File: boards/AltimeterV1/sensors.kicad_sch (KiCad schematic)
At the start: 23 parts

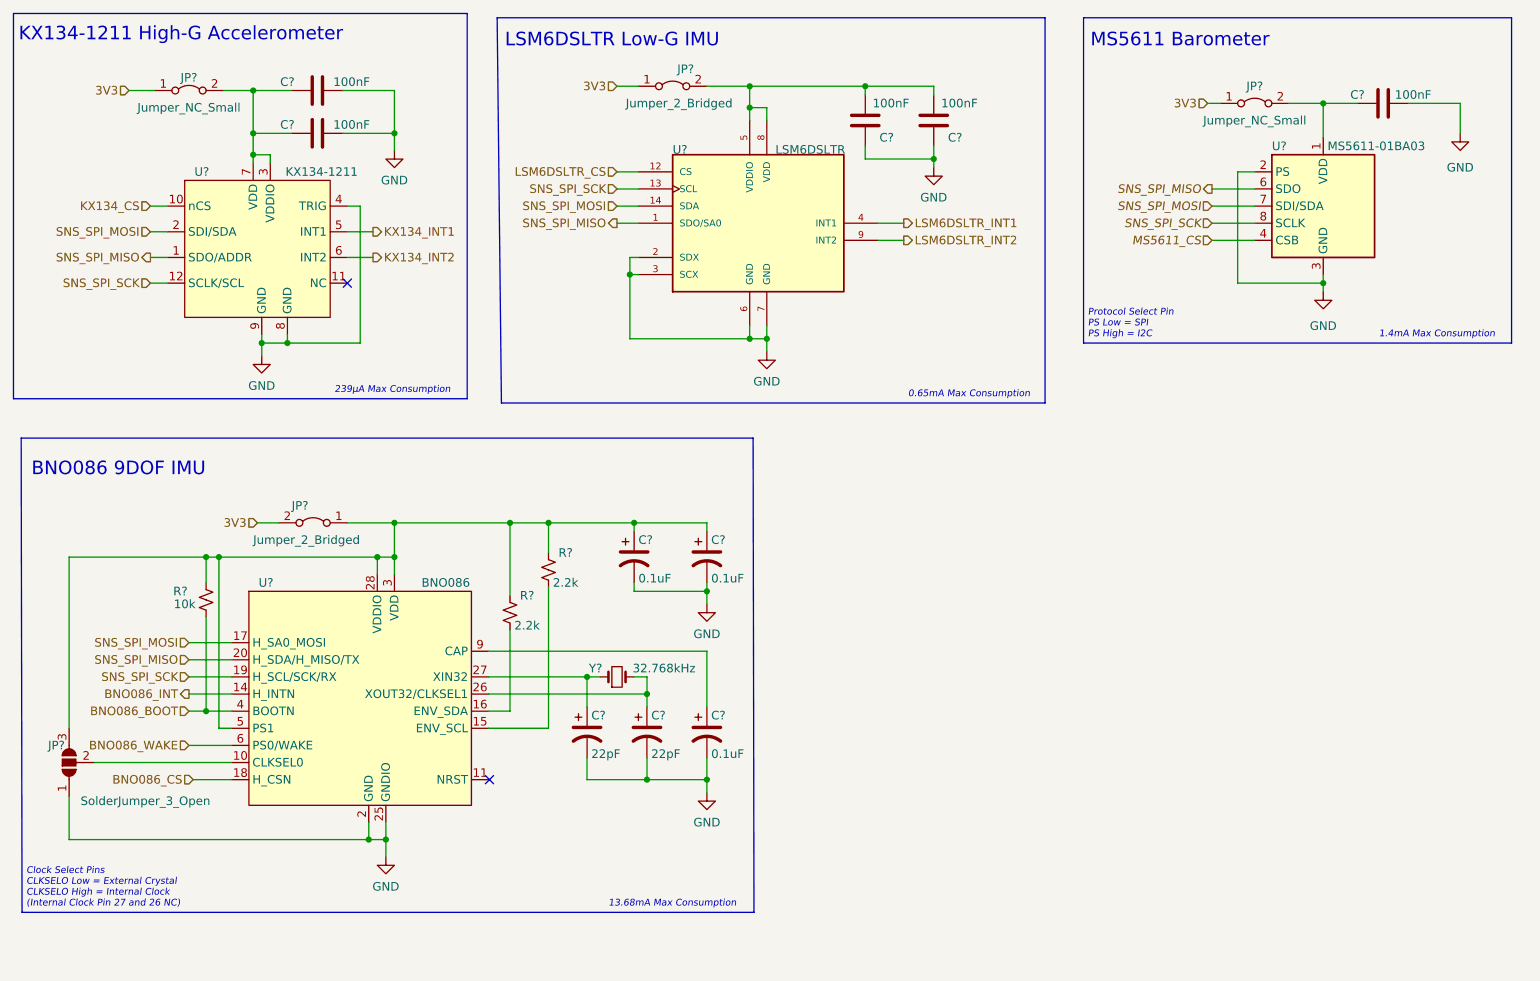
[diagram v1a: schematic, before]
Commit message: updated sensor schematics for I2C communication, added SNS I2C labels for MCU and headers
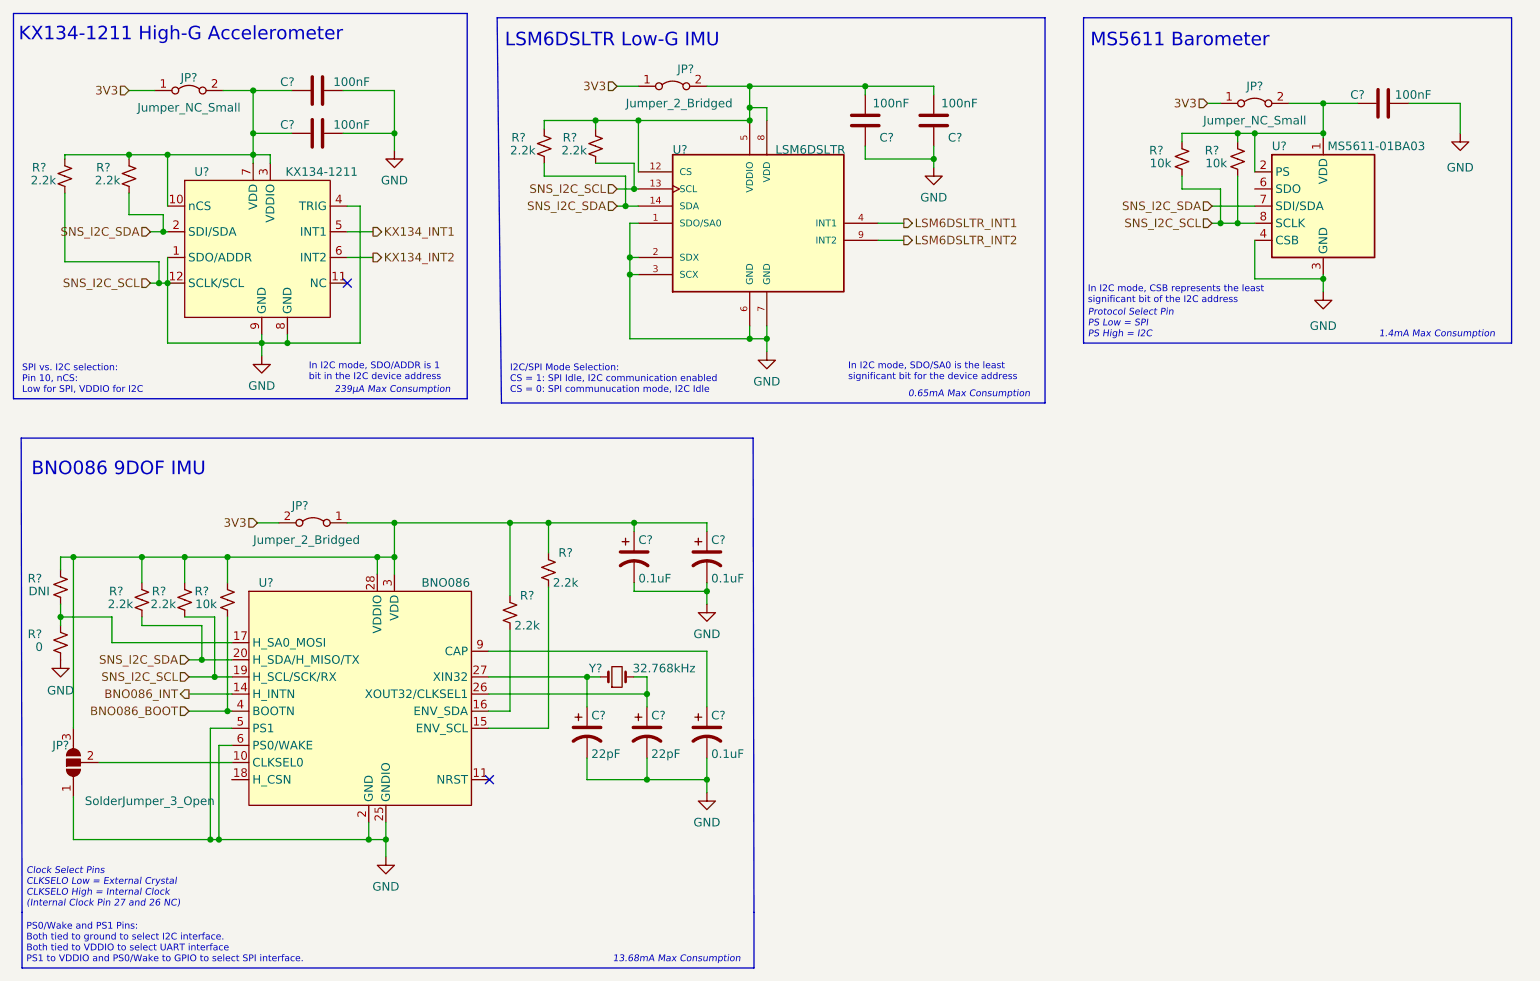
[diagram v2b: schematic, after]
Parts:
- added R? (x6): 2.2k, Resistor_SMD:R_0805_2012Metric_Pad1.20x1.40mm_HandSolder, symbol Device:R_Small_US
- added R?: DNI, Resistor_SMD:R_0805_2012Metric_Pad1.20x1.40mm_HandSolder, symbol Device:R_Small_US
- added R?: 0, Resistor_SMD:R_0805_2012Metric_Pad1.20x1.40mm_HandSolder, symbol Device:R_Small_US
- added R? (x2): 10k, Resistor_SMD:R_0805_2012Metric_Pad1.20x1.40mm_HandSolder, symbol Device:R_Small_US
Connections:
- net BNO086_WAKE is gone; now on net GND: U?.6 (PS0/WAKE)
- net KX134_CS is gone; now on an unnamed net: U?.10 (nCS)
- net LSM6DSLTR_CS is gone; now on an unnamed net: U?.12 (CS)
- net MS5611_CS is gone; now on net GND: U?.4 (CSB), U?.5 (CSB)
- net SNS_SPI_SCK is gone; now on net GND: U?.12 (SCLK/SCL), U?.13 (SCL), U?.19 (H_SCL/SCK/RX), U?.8 (SCLK)
- net GND: now also U?.1 (SDO/ADDR), U?.1 (SDO/SA0), U?.5 (PS1), R?.1, R?.1, R?.1, R?.1, R?.1, R?.1; no longer U?.2 (PS)
- net at C?.1, C?.2, JP?.2 (B)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: now also R?.2, R?.2
- net at C?.2, C?.2, JP?.2 (B)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: now also R?.2, R?.2
- net at C?.2, JP?.2 (B), U?.1 (VDD): now also U?.2 (PS), R?.2, R?.2
- net at C?.1, C?.1, JP?.1 (A)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: now also R?.2, R?.2, R?.2; no longer U?.5 (PS1)
- net BNO086_CS: no longer names the net of U?.18 (H_CSN)
- removed net SNS_SPI_MISO: U?.1 (SDO/ADDR), U?.1 (SDO/SA0), U?.20 (H_SDA/H_MISO/TX), U?.6 (SDO)
- net SNS_SPI_MOSI renamed SNS_I2C_SDA
- net SNS_I2C_SDA: now also U?.20 (H_SDA/H_MISO/TX), R?.1, R?.1, R?.1; no longer U?.17 (H_SA0_MOSI)
- new net: R?.1, R?.2, U?.17 (H_SA0_MOSI)
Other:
- note added: "I2C/SPI Mode Selection: CS = 1: SPI Idle, I2C communication enabled CS = 0: SPI communucation mode, I2C Idle"
- note added: "In I2C mode, CSB represents the least significant bit of the I2C address"
- note added: "In I2C mode, SDO/ADDR is 1 bit in the I2C device address"
- note added: "In I2C mode, SDO/SA0 is the least significant bit for the device address"
- note added: "PS0/Wake and PS1 Pins: Both tied to ground to select I2C interface. Both tied to VDDIO to select UART interface PS1 to VDDIO and PS0/Wake to GPIO to select SPI interface."
- note added: "SPI vs. I2C selection: Pin 10, nCS: Low for SPI, VDDIO for I2C"
- moved on the sheet: JP?, R?

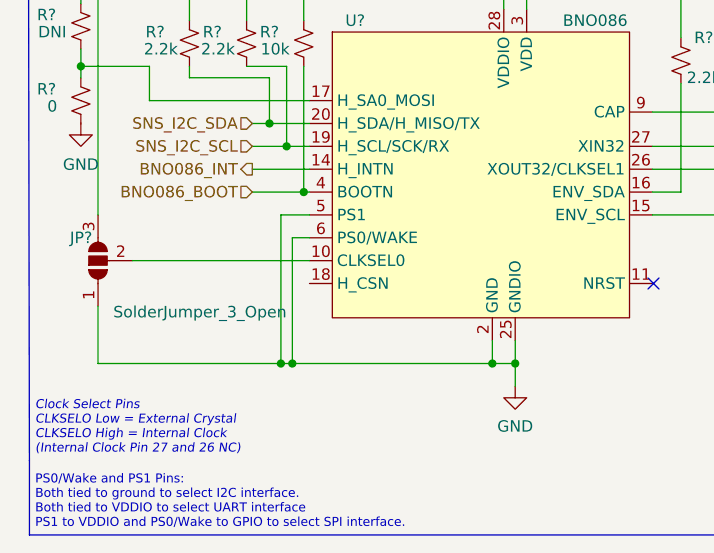
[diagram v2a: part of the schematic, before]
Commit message: updated hierarchical sheets and moved power schematics
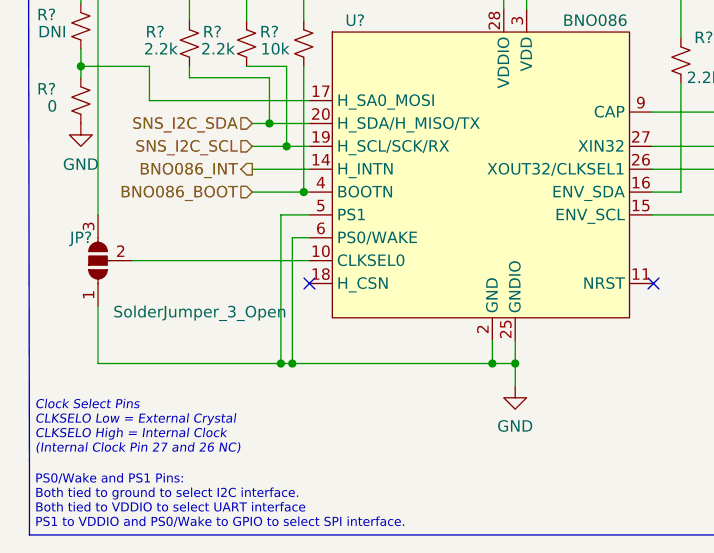
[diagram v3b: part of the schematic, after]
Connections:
- no-connect marks 2 -> 3
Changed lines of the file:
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@@
   (junction (at 107.95 54.61) (diameter 0) (color 0 0 0 0)
   )
+  (no_connect (at 48.895 129.54))
   (no_connect (at 87.122 129.54))
   (no_connect (at 66.04 55.88))

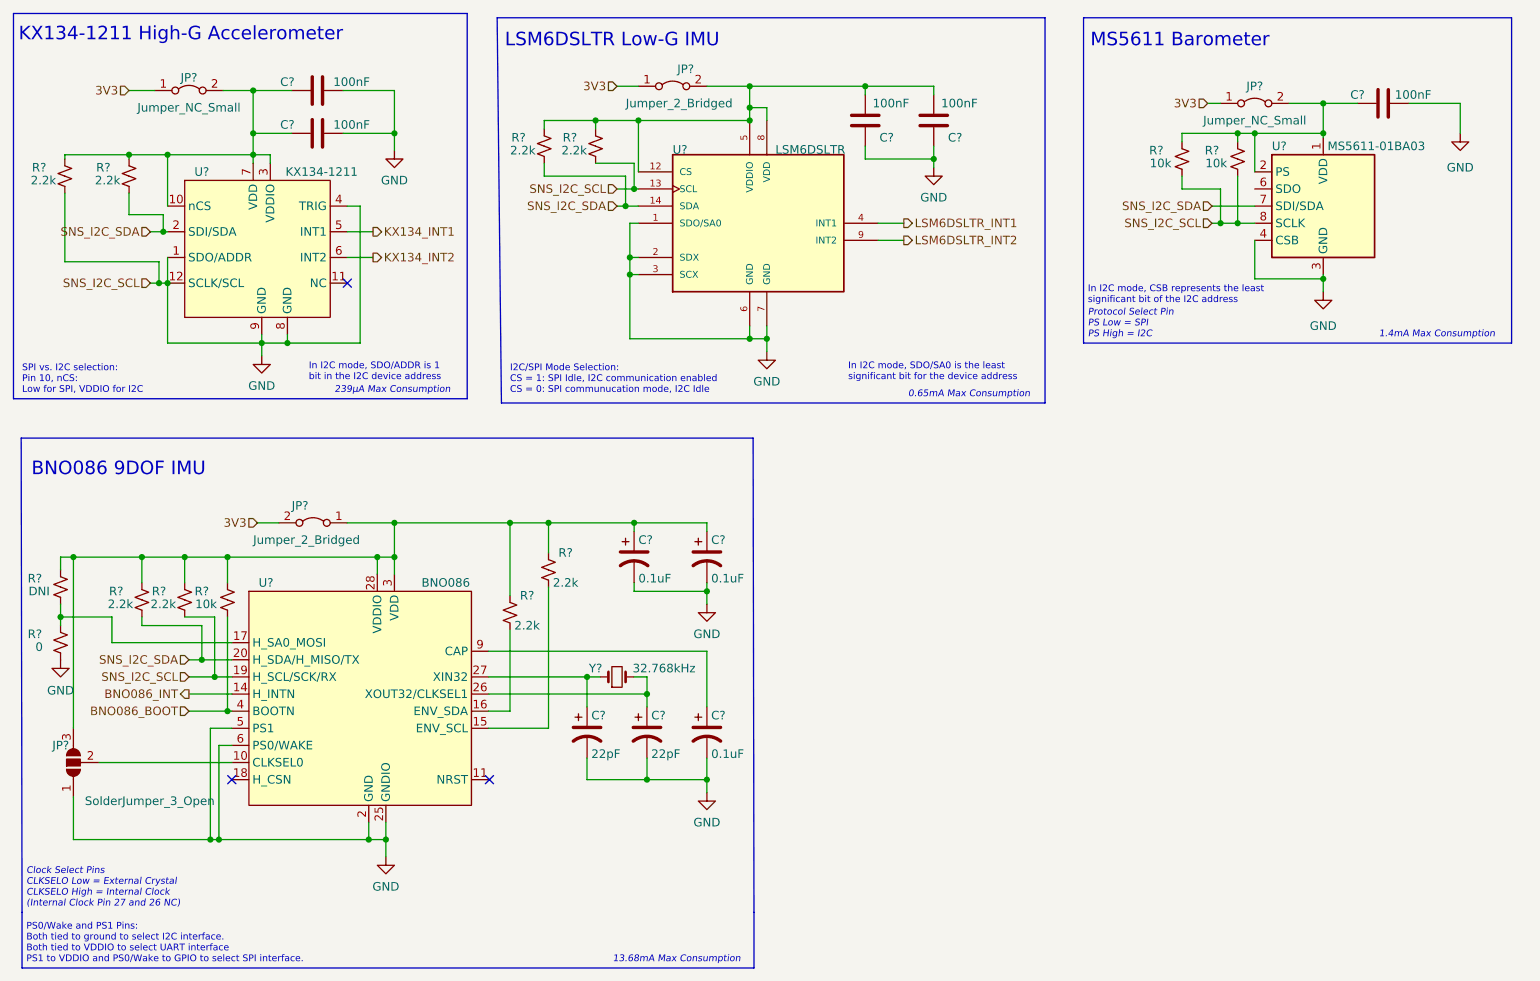
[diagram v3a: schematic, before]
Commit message: added flash memory, added buzzer, corrected all schematic labels, assigned footprints, added switch, updated pcb from schematic
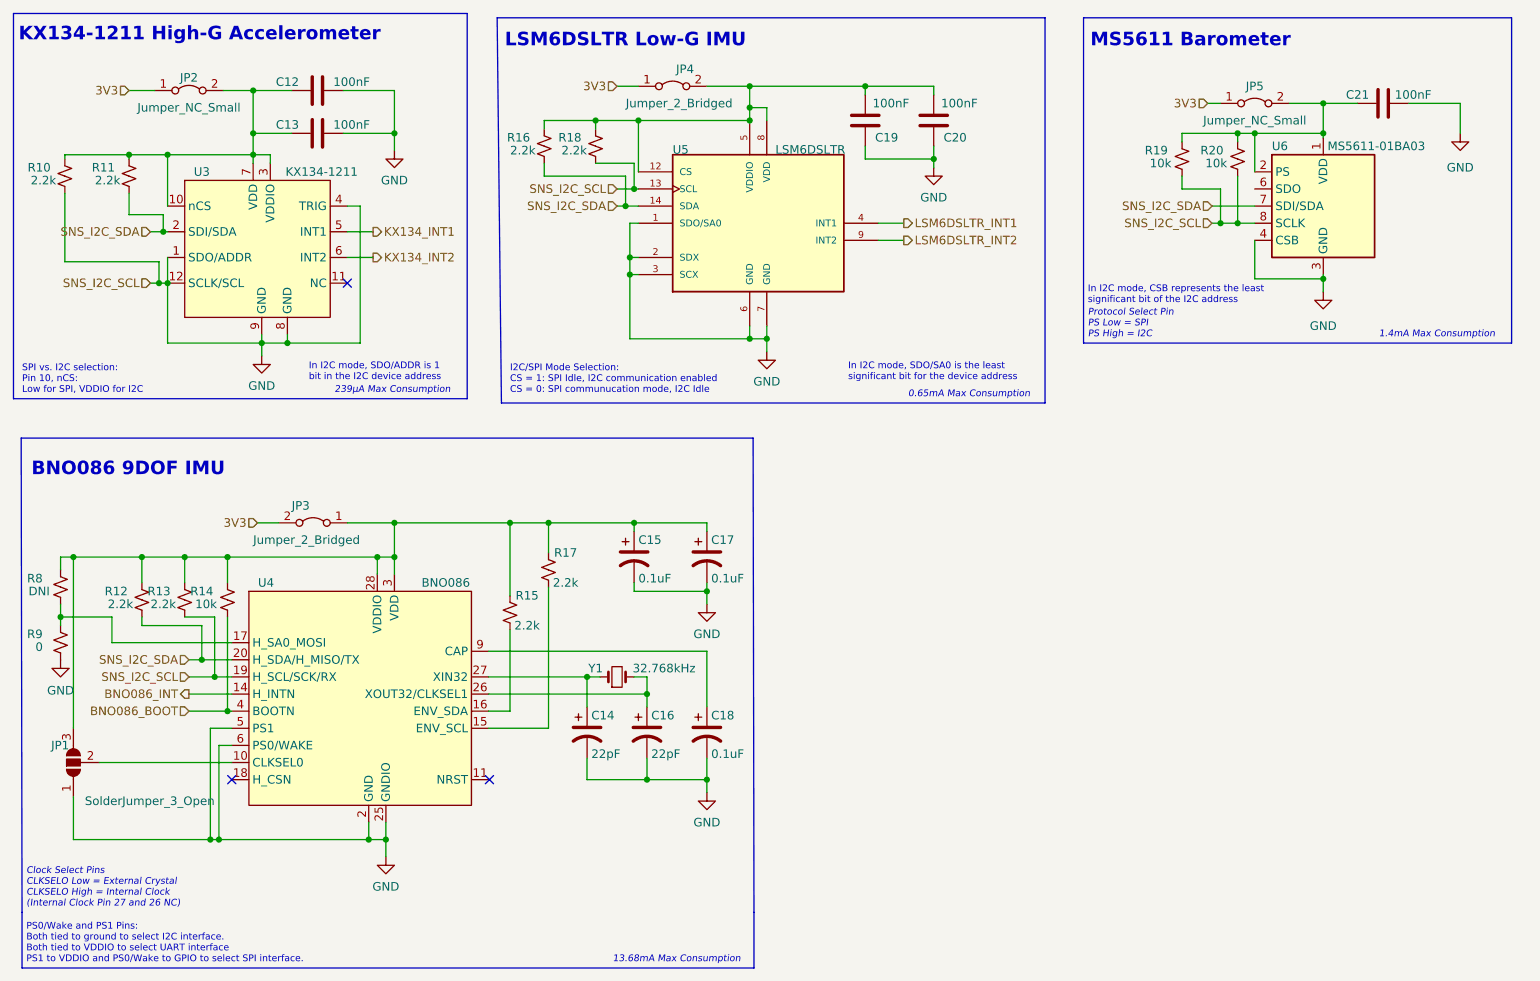
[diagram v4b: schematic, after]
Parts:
- gave numbers to parts that had none: 33
